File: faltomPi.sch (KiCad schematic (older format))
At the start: 0 parts

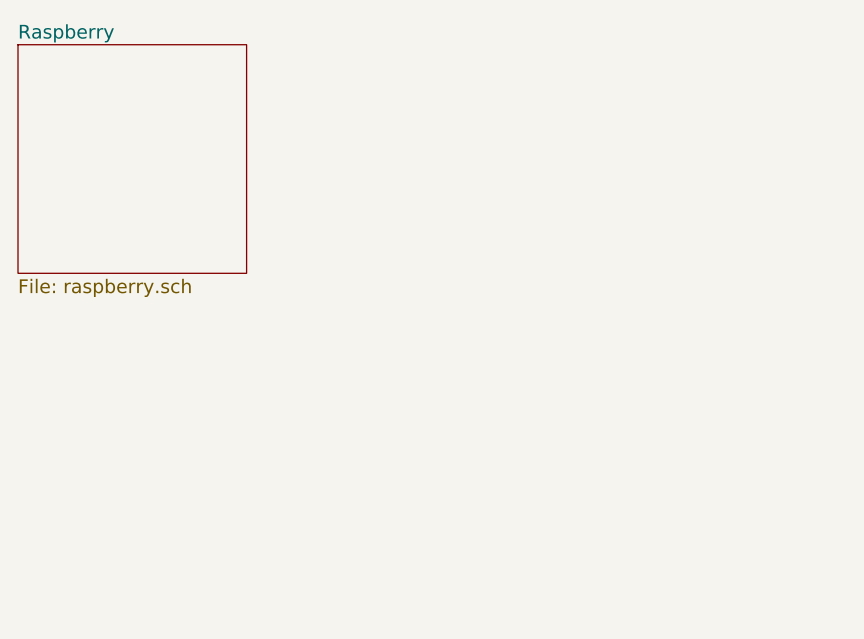
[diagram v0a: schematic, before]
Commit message: Add DigitalIO connector
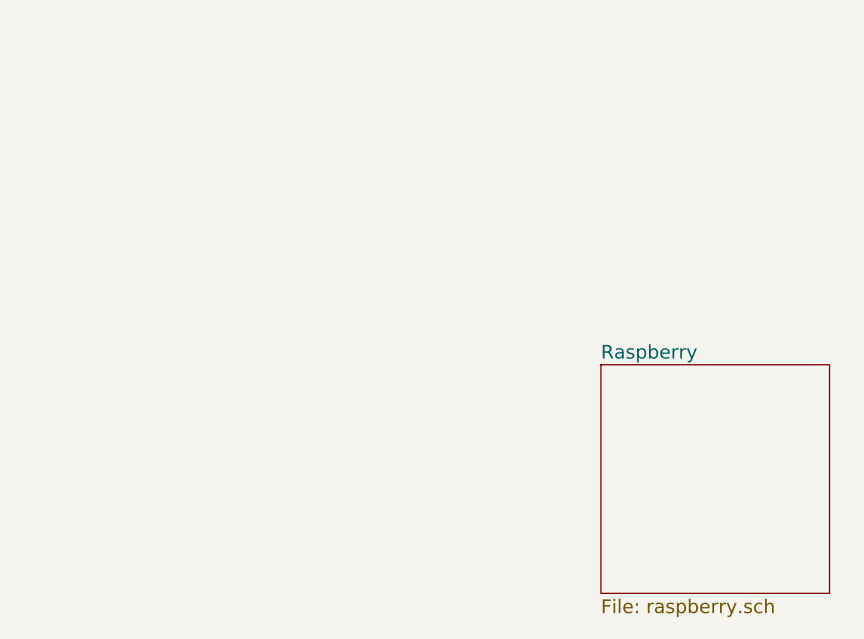
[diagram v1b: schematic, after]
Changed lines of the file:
@@
 $EndDescr
 $Sheet
-S 1400 1400 1000 1000
+S 3950 2800 1000 1000
 U 5515D395
 F0 "Raspberry" 60
